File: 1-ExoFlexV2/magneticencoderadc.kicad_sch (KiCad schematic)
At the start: 0 parts

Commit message: Finalisation schéma FIN
- Changement des uméro pour les inverseurs
- Changement des connecteur et début de placement
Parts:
- added J55, J56, J58, J59, J66, J67: Jumper, Connector_PinHeader_2.54mm:PinHeader_1x03_P2.54mm_Vertical, symbol Connector:Conn_01x03_Male
- added R178, R179, R180, R52, R68, R69, R70, R77, R78, R95, R96, R97: 3.3k 1% 1/8W, Resistor_SMD:R_0805_2012Metric, symbol Device:R_Small_US
- added R181, R186, R187, R79, R80, R81: 0Ω, Resistor_SMD:R_0805_2012Metric, symbol Device:R_Small_US
- added R188, R189, R190, R191, R192, R193, R49, R50, R51, R82, R83, R84, R85, R86, R87, R92, R93, R94: 10K 1% 1/10W, Resistor_SMD:R_0603_1608Metric, symbol Device:R_Small_US
- added R194, R195, R196, R88, R90, R91: 100k 1% 1/20W, Resistor_SMD:R_0201_0603Metric, symbol Device:R_Small_US
- added U17, U18, U19, U23, U24, U31: OP_AMP2, FootPrintLib:SOIC127P599X175-8N, symbol SymLib:TL072IDR
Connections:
- new net: R78.2, R81.1
- new net: R81.2, R86.2, U19.1 (1OUT)
- new net: R51.2, R69.1, U19.2 (1IN-)
- new net: R187.2, R192.2, U31.1 (1OUT)
- new net: R94.2, R97.1, U31.2 (1IN-)
- new net: R192.1, R193.2, U31.6 (2IN-)
- new net: J67.1 (Pin_1), R193.1, U31.7 (2OUT)
- new net: R190.1, R191.2, U24.6 (2IN-)
- new net: R186.2, R190.2, U24.1 (1OUT)
- new net: J55.1 (Pin_1), R83.1, U17.7 (2OUT)
- new net: R82.1, R83.2, U17.6 (2IN-)
- new net: R86.1, R87.2, U19.6 (2IN-)
- new net: J58.1 (Pin_1), R87.1, U19.7 (2OUT)
- new net: R180.1, R97.2
- new net: R69.2, R78.1
- new net: J66.1 (Pin_1), R191.1, U24.7 (2OUT)
- new net: J66.3 (Pin_3), R195.1
- new net: R52.2, R70.1
- new net: R70.2, R79.1
- new net: R178.2, R181.1
- new net: R181.2, R188.2, U23.1 (1OUT)
- new net: J59.1 (Pin_1), R189.1, U23.7 (2OUT)
- new net: R188.1, R189.2, U23.6 (2IN-)
- new net: R77.2, R80.1
- new net: R80.2, R84.2, U18.1 (1OUT)
- new net: R93.2, R96.1, U24.2 (1IN-)
- new net: R178.1, R95.2
- new net: J56.3 (Pin_3), R90.1
- new net: R84.1, R85.2, U18.6 (2IN-)
- new net: R49.2, R52.1, U17.2 (1IN-)
- new net: R50.2, R68.1, U18.2 (1IN-)
- new net: R68.2, R77.1
- new net: R79.2, R82.2, U17.1 (1OUT)
- new net: R92.2, R95.1, U23.2 (1IN-)
- new net: J56.1 (Pin_1), R85.1, U18.7 (2OUT)
- new net: R180.2, R187.1
- new net: J55.3 (Pin_3), R88.1
- new net: J59.3 (Pin_3), R194.1
- new net: J58.3 (Pin_3), R91.1
- new net: R179.2, R186.1
- new net: R179.1, R96.2
- new net: J67.3 (Pin_3), R196.1
- new net +5VA: U17.8 (VCC+), U18.8 (VCC+), U19.8 (VCC+), U23.8 (VCC+), U24.8 (VCC+), U31.8 (VCC+)
- new net -5VA: U17.4 (VCC-), U18.4 (VCC-), U19.4 (VCC-), U23.4 (VCC-), U24.4 (VCC-), U31.4 (VCC-)
- new net DOR_AMP_DATA: J58.2 (Pin_2)
- new net DOR_AMP_DATA1: R51.1
- new net DOR_AMP_LIM_DATA: J59.2 (Pin_2)
- new net DOR_AMP_LIM_DATA1: R92.1
- new net EVE_AMP_DATA: J55.2 (Pin_2)
- new net EVE_AMP_DATA1: R49.1
- new net EVE_AMP_LIM_DATA: J56.2 (Pin_2)
- new net EVE_AMP_LIM_DATA1: R50.1
- new net EXT_AMP_DATA: J66.2 (Pin_2)
- new net EXT_AMP_DATA1: R93.1
- new net EXT_AMP_LIM_DATA: J67.2 (Pin_2)
- new net EXT_AMP_LIM_DATA1: R94.1
- new net GND: R194.2, R195.2, R196.2, R88.2, R90.2, R91.2, U17.3 (1IN+), U17.5 (2IN+), U18.3 (1IN+), U18.5 (2IN+), U19.3 (1IN+), U19.5 (2IN+), U23.3 (1IN+), U23.5 (2IN+), U24.3 (1IN+), U24.5 (2IN+), U31.3 (1IN+), U31.5 (2IN+)
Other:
- note added: "-3,3-0V"
- note added: "0-3,3V"
- note added: "0-5V"
- note added: "12xOP : 5VA @ 30mA Total current : 5VA @ 30mA"
- note added: "NOTES:"
- note added: "Topologie : - Atténuateur pour passer de 0-5V à 3,3V - Gain négatif pour inverser le signal de l'atténuateur (Ampli-OP inverseur)"

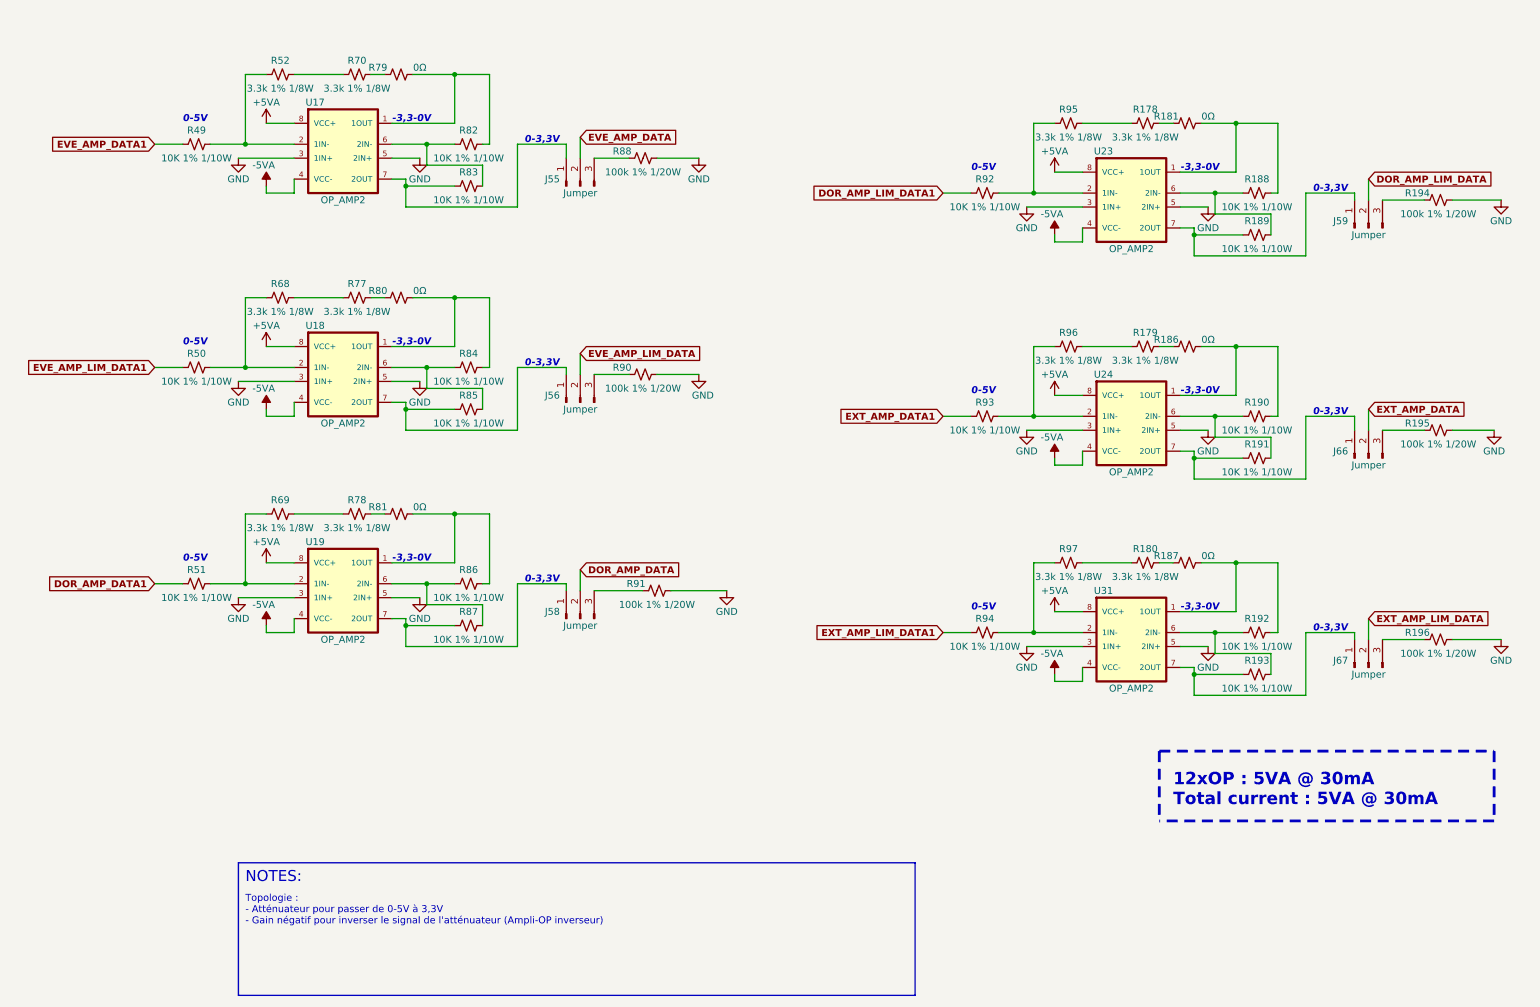
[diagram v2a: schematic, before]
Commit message: Modification Schéma + Layout
- Ajout de RC potentiel entre les capteur de torque et l'ampli d'instru
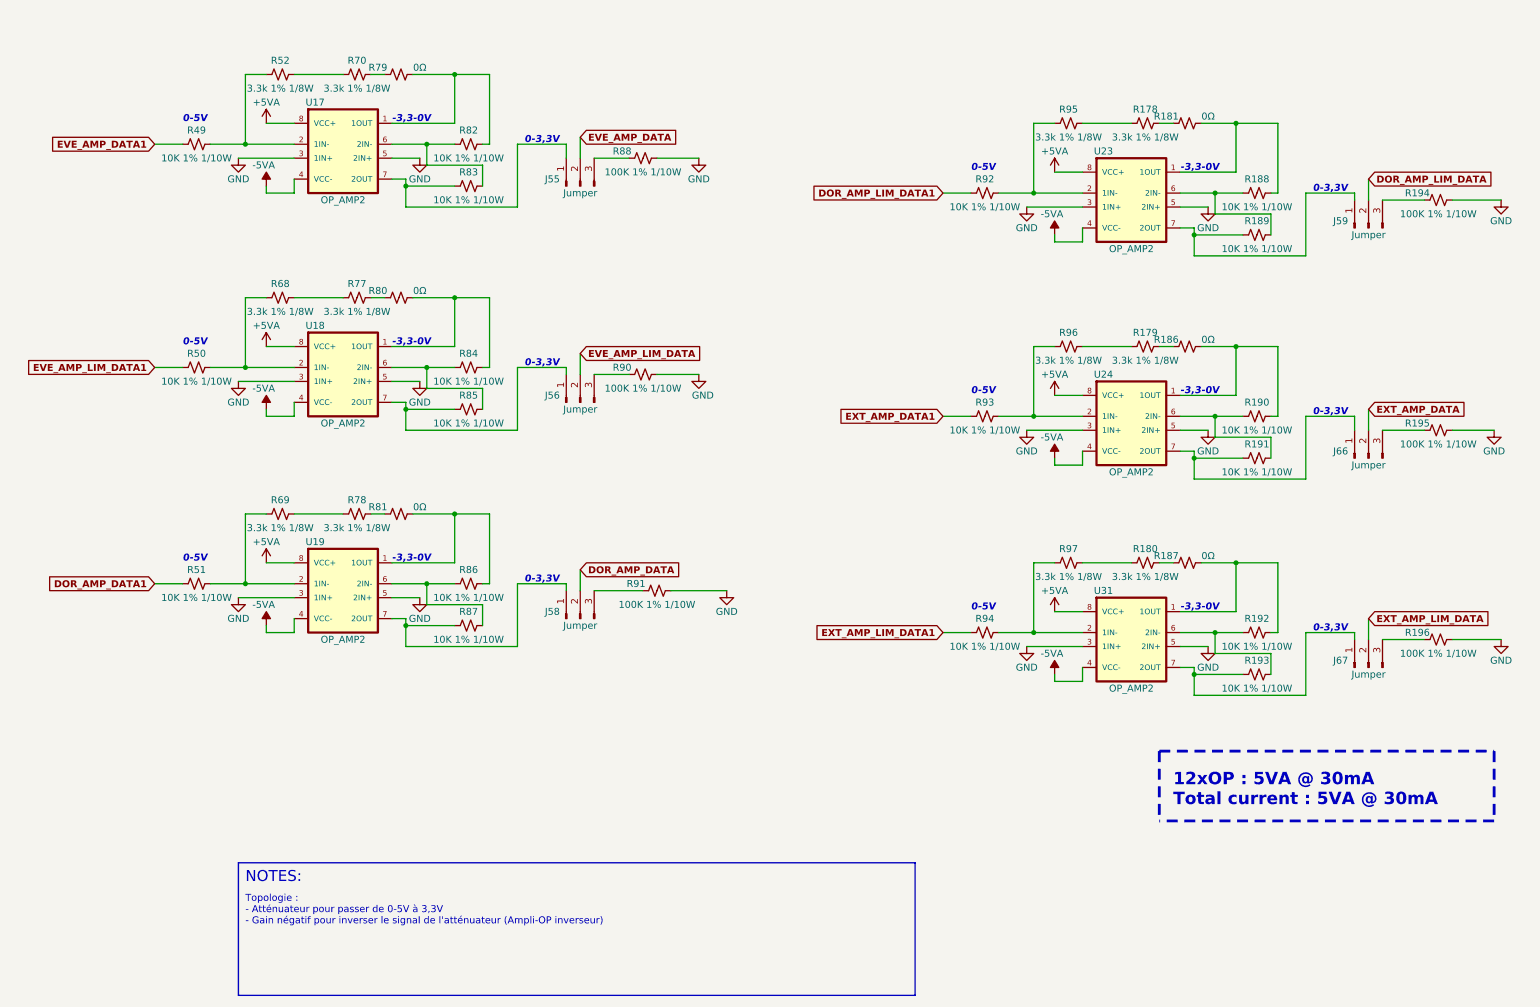
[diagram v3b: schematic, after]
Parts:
- R194, R195, R196, R88, R90, R91: value 100k 1% 1/20W -> 100K 1% 1/10W; footprint Resistor_SMD:R_0201_0603Metric -> Resistor_SMD:R_0603_1608Metric; DESCRIPTION 100 kOhms ±1% 0.05W, 1/20W Chip Resistor 0201 (0603 Metric)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 -> 100 kOhms ±1% 0.1W, 1/10W Chip Resistor 0603 (1608 Metric) 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
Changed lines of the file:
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@@
     (in_bom yes) (on_board yes)
     (property "Reference" "R195" (id 0) (at 264.16 91.44 90))
-    (property "Value" "100k 1% 1/20W" (id 1) (at 267.97 95.25 90))
-    (property "Footprint" "Resistor_SMD:R_0201_0603Metric" (id 2) (at 267.97 92.71 0)
+    (property "Value" "100K 1% 1/10W" (id 1) (at 267.97 95.25 90))
+    (property "Footprint" "Resistor_SMD:R_0603_1608Metric" (id 2) (at 267.97 92.71 0)
       (effects (font (size 1.27 1.27)) hide)
     )
@@
       (effects (font (size 1.27 1.27)) hide)
     )
-    (property "DESCRIPTION" "100 kOhms ±1% 0.05W, 1/20W Chip Resistor 0201 (0603 Metric) Thick Film" (id 8) (at 267.97 92.71 0)
+    (property "DESCRIPTION" "100 kOhms ±1% 0.1W, 1/10W Chip Resistor 0603 (1608 Metric) Automotive AEC-Q200 Thick Film" (id 8) (at 267.97 92.71 0)
       (effects (font (size 1.27 1.27)) hide)
     )
@@
     (in_bom yes) (on_board yes)
     (property "Reference" "R90" (id 0) (at 119.38 81.28 90))
-    (property "Value" "100k 1% 1/20W" (id 1) (at 123.19 85.09 90))
-    (property "Footprint" "Resistor_SMD:R_0201_0603Metric" (id 2) (at 123.19 82.55 0)
+    (property "Value" "100K 1% 1/10W" (id 1) (at 123.19 85.09 90))
+    (property "Footprint" "Resistor_SMD:R_0603_1608Metric" (id 2) (at 123.19 82.55 0)
       (effects (font (size 1.27 1.27)) hide)
     )
@@
       (effects (font (size 1.27 1.27)) hide)
     )
-    (property "DESCRIPTION" "100 kOhms ±1% 0.05W, 1/20W Chip Resistor 0201 (0603 Metric) Thick Film" (id 8) (at 123.19 82.55 0)
+    (property "DESCRIPTION" "100 kOhms ±1% 0.1W, 1/10W Chip Resistor 0603 (1608 Metric) Automotive AEC-Q200 Thick Film" (id 8) (at 123.19 82.55 0)
       (effects (font (size 1.27 1.27)) hide)
     )
@@
     (in_bom yes) (on_board yes)
     (property "Reference" "R88" (id 0) (at 119.38 41.91 90))
-    (property "Value" "100k 1% 1/20W" (id 1) (at 123.19 45.72 90))
-    (property "Footprint" "Resistor_SMD:R_0201_0603Metric" (id 2) (at 123.19 43.18 0)
+    (property "Value" "100K 1% 1/10W" (id 1) (at 123.19 45.72 90))
+    (property "Footprint" "Resistor_SMD:R_0603_1608Metric" (id 2) (at 123.19 43.18 0)
       (effects (font (size 1.27 1.27)) hide)
     )
@@
       (effects (font (size 1.27 1.27)) hide)
     )
-    (property "DESCRIPTION" "100 kOhms ±1% 0.05W, 1/20W Chip Resistor 0201 (0603 Metric) Thick Film" (id 8) (at 123.19 43.18 0)
+    (property "DESCRIPTION" "100 kOhms ±1% 0.1W, 1/10W Chip Resistor 0603 (1608 Metric) Automotive AEC-Q200 Thick Film" (id 8) (at 123.19 43.18 0)
       (effects (font (size 1.27 1.27)) hide)
     )
@@
     (in_bom yes) (on_board yes)
     (property "Reference" "R91" (id 0) (at 121.92 120.65 90))
-    (property "Value" "100k 1% 1/20W" (id 1) (at 125.73 124.46 90))
-    (property "Footprint" "Resistor_SMD:R_0201_0603Metric" (id 2) (at 125.73 121.92 0)
+    (property "Value" "100K 1% 1/10W" (id 1) (at 125.73 124.46 90))
+    (property "Footprint" "Resistor_SMD:R_0603_1608Metric" (id 2) (at 125.73 121.92 0)
       (effects (font (size 1.27 1.27)) hide)
     )
@@
       (effects (font (size 1.27 1.27)) hide)
     )
-    (property "DESCRIPTION" "100 kOhms ±1% 0.05W, 1/20W Chip Resistor 0201 (0603 Metric) Thick Film" (id 8) (at 125.73 121.92 0)
+    (property "DESCRIPTION" "100 kOhms ±1% 0.1W, 1/10W Chip Resistor 0603 (1608 Metric) Automotive AEC-Q200 Thick Film" (id 8) (at 125.73 121.92 0)
       (effects (font (size 1.27 1.27)) hide)
     )
@@
     (in_bom yes) (on_board yes)
     (property "Reference" "R196" (id 0) (at 264.16 129.54 90))
-    (property "Value" "100k 1% 1/20W" (id 1) (at 267.97 133.35 90))
-    (property "Footprint" "Resistor_SMD:R_0201_0603Metric" (id 2) (at 267.97 130.81 0)
+    (property "Value" "100K 1% 1/10W" (id 1) (at 267.97 133.35 90))
+    (property "Footprint" "Resistor_SMD:R_0603_1608Metric" (id 2) (at 267.97 130.81 0)
       (effects (font (size 1.27 1.27)) hide)
     )
@@
       (effects (font (size 1.27 1.27)) hide)
     )
-    (property "DESCRIPTION" "100 kOhms ±1% 0.05W, 1/20W Chip Resistor 0201 (0603 Metric) Thick Film" (id 8) (at 267.97 130.81 0)
+    (property "DESCRIPTION" "100 kOhms ±1% 0.1W, 1/10W Chip Resistor 0603 (1608 Metric) Automotive AEC-Q200 Thick Film" (id 8) (at 267.97 130.81 0)
       (effects (font (size 1.27 1.27)) hide)
     )
@@
     (in_bom yes) (on_board yes)
     (property "Reference" "R194" (id 0) (at 264.16 49.53 90))
-    (property "Value" "100k 1% 1/20W" (id 1) (at 267.97 53.34 90))
-    (property "Footprint" "Resistor_SMD:R_0201_0603Metric" (id 2) (at 267.97 50.8 0)
+    (property "Value" "100K 1% 1/10W" (id 1) (at 267.97 53.34 90))
+    (property "Footprint" "Resistor_SMD:R_0603_1608Metric" (id 2) (at 267.97 50.8 0)
       (effects (font (size 1.27 1.27)) hide)
     )
@@
       (effects (font (size 1.27 1.27)) hide)
     )
-    (property "DESCRIPTION" "100 kOhms ±1% 0.05W, 1/20W Chip Resistor 0201 (0603 Metric) Thick Film" (id 8) (at 267.97 50.8 0)
-      (effects (font (size 1.27 1.27)) hide)
-    )
+    (property "DESCRIPTION" "100 kOhms ±1% 0.1W, 1/10W Chip Resistor 0603 (1608 Metric) Automotive AEC-Q200 Thick Film" (id 8) (at 267.97 50.8 0)
+      (effects (font (size 1.27 1.27)) hide)
+    )

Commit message: Routage pour Review 1
- Replacement des test point pour faciliter le rework
- Correction des erreurs dans le BOM
-
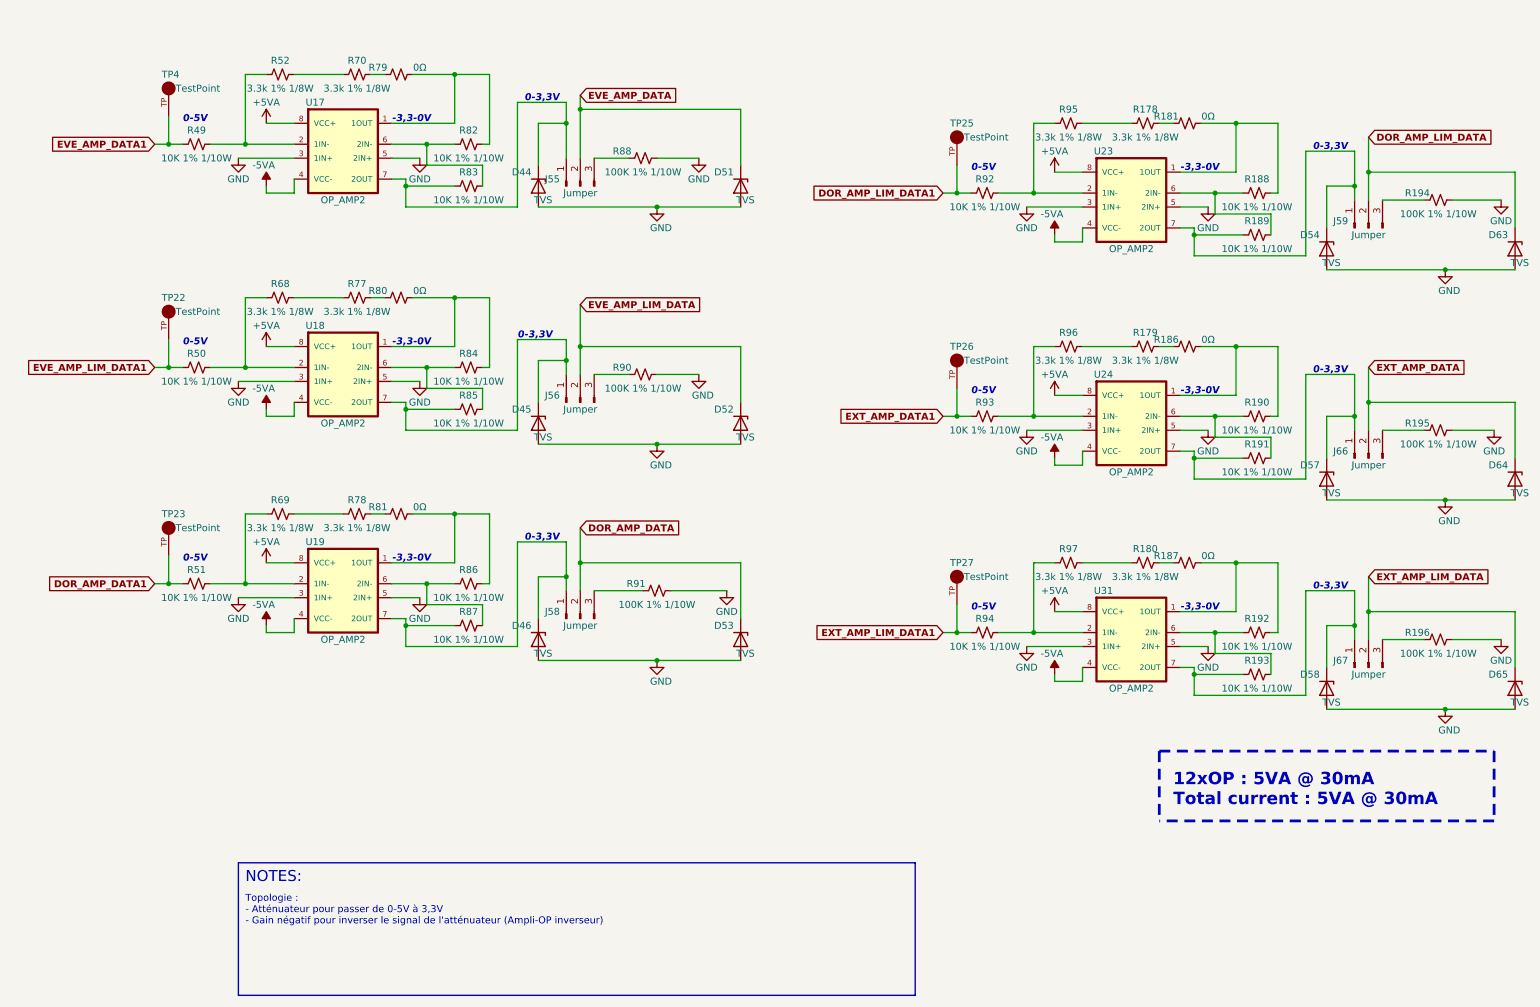
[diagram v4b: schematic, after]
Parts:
- added D44, D45, D46, D51, D52, D53, D54, D57, D58, D63, D64, D65: TVS, FootPrint:DPY2_TEX, symbol Device:D_Zener
- added TP22, TP23, TP25, TP26, TP27, TP4: TestPoint, FootPrint:KEYSTONE_5005, symbol SymLib:5005
- R194, R195, R196, R88, R90, R91: PACKAGE 0201 (0603 Metric) -> 0603 (1608 Metric); PART NUMBER ERJ-1GNF1003C -> ERJ-3EKF1003V
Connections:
- net DOR_AMP_DATA: now also D53.1 (K)
- net DOR_AMP_DATA1: now also TP23.TP
- net DOR_AMP_LIM_DATA: now also D63.1 (K)
- net DOR_AMP_LIM_DATA1: now also TP25.TP
- net EVE_AMP_DATA: now also D51.1 (K)
- net EVE_AMP_DATA1: now also TP4.TP
- net EVE_AMP_LIM_DATA: now also D52.1 (K)
- net EVE_AMP_LIM_DATA1: now also TP22.TP
- net EXT_AMP_DATA: now also D64.1 (K)
- net EXT_AMP_DATA1: now also TP26.TP
- net EXT_AMP_LIM_DATA: now also D65.1 (K)
- net EXT_AMP_LIM_DATA1: now also TP27.TP
- net GND: now also D44.2 (A), D45.2 (A), D46.2 (A), D51.2 (A), D52.2 (A), D53.2 (A), D54.2 (A), D57.2 (A), D58.2 (A), D63.2 (A), D64.2 (A), D65.2 (A)
- net at J67.1 (Pin_1), R193.1, U31.7 (2OUT): now also D58.1 (K)
- net at J55.1 (Pin_1), R83.1, U17.7 (2OUT): now also D44.1 (K)
- net at J58.1 (Pin_1), R87.1, U19.7 (2OUT): now also D46.1 (K)
- net at J66.1 (Pin_1), R191.1, U24.7 (2OUT): now also D57.1 (K)
- net at J59.1 (Pin_1), R189.1, U23.7 (2OUT): now also D54.1 (K)
- net at J56.1 (Pin_1), R85.1, U18.7 (2OUT): now also D45.1 (K)
